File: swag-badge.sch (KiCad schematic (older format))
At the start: 7 parts

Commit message: Removed tinypico footprint :(
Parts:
- removed J?: Lolin32_Header_Left, symbol Connector_Generic:Conn_01x16
- removed J?: Lolin32_Header_Right, symbol Connector_Generic:Conn_01x20
- removed LEFT1, RIGHT1: TINYPICO_HEADER_10, Shield_Empty:1X10_NO_SILK, symbol swag-badge-rescue:TINYPICO_HEADER_10NO_SILK_PTH_FEMALE-Shield_Empty-eagle-import
- added J6: SAO_2, Pin_Headers:Pin_Header_Straight_2x03_Pitch2.54mm, symbol Connector_Generic:Conn_02x03_Counter_Clockwise
- added J?: Lolin32, symbol Connector_Generic:Conn_02x13_Counter_Clockwise
- added J?: SAO_3, Pin_Headers:Pin_Header_Straight_2x03_Pitch2.54mm, symbol Connector_Generic:Conn_02x03_Counter_Clockwise
- J1, J2: renamed from J?; footprint (none) -> Pin_Headers:Pin_Header_Straight_1x04_Pitch2.54mm
- J5: renamed from J?; footprint (none) -> Pin_Headers:Pin_Header_Straight_2x03_Pitch2.54mm
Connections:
- net labels added: EN, GPIO0, GPIO12, GPIO13, GPIO16, GPIO17, GPIO2, GPIO34, GPIO35, VN, VP
- net labels removed: +5V, 3.3V, GPIO21, RESET, USB, VBAT
- wire segments 44 -> 64
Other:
- moved on the sheet: J1, J2, J5

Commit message: Footprints associated
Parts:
- J1, J2: footprint Pin_Headers:Pin_Header_Straight_1x04_Pitch2.54mm -> SwagBadge:Display_Module_128X64_I2C_SSD1306
- J3: renamed from J?; footprint (none) -> SwagBadge:LOLIN32_Flipped_SmallCut
- J4: renamed from J?; footprint Pin_Headers:Pin_Header_Straight_2x03_Pitch2.54mm -> SwagBadge:SAO_Header_6-Pin
- J5, J6: footprint Pin_Headers:Pin_Header_Straight_2x03_Pitch2.54mm -> SwagBadge:SAO_Header_6-Pin
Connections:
- net +3V3: now also J3.14 (Pin_14); no longer J3.26 (Pin_26)
- net EN: now also J3.11 (Pin_11); no longer J3.3 (Pin_3)
- net GND: now also J3.1 (Pin_1); no longer J3.13 (Pin_13)
- net GPIO0: now also J3.23 (Pin_23); no longer J3.17 (Pin_17)
- net GPIO12: now also J3.2 (Pin_2); no longer J3.12 (Pin_12)
- net GPIO13: now also J3.26 (Pin_26); no longer J3.14 (Pin_14)
- net GPIO14: now also J3.3 (Pin_3); no longer J3.11 (Pin_11)
- net GPIO15: now also J3.25 (Pin_25); no longer J3.15 (Pin_15)
- net GPIO16: now also J3.21 (Pin_21); no longer J3.19 (Pin_19)
- net GPIO18: now also J3.18 (Pin_18); no longer J3.22 (Pin_22)
- net GPIO19: now also J3.16 (Pin_16); no longer J3.24 (Pin_24)
- net GPIO2: now also J3.24 (Pin_24); no longer J3.16 (Pin_16)
- net GPIO22: now also J3.15 (Pin_15); no longer J3.25 (Pin_25)
- net GPIO23: now also J3.17 (Pin_17); no longer J3.23 (Pin_23)
- net GPIO25: now also J3.6 (Pin_6); no longer J3.8 (Pin_8)
- net GPIO26: now also J3.5 (Pin_5); no longer J3.9 (Pin_9)
- net GPIO27: now also J3.4 (Pin_4); no longer J3.10 (Pin_10)
- net GPIO32: now also J3.8 (Pin_8); no longer J3.6 (Pin_6)
- net GPIO34: now also J3.10 (Pin_10); no longer J3.4 (Pin_4)
- net GPIO35: now also J3.9 (Pin_9); no longer J3.5 (Pin_5)
- net GPIO4: now also J3.22 (Pin_22); no longer J3.18 (Pin_18)
- net GPIO5: now also J3.19 (Pin_19); no longer J3.21 (Pin_21)
- net VN: now also J3.12 (Pin_12); no longer J3.2 (Pin_2)
- net VP: now also J3.13 (Pin_13); no longer J3.1 (Pin_1)
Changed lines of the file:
@@
 F 0 "J1" H 3268 4867 50  0000 C CNN
 F 1 "OLED_1" H 3268 4776 50  0000 C CNN
-F 2 "Pin_Headers:Pin_Header_Straight_1x04_Pitch2.54mm" H 3350 4550 50  0001 C CNN
+F 2 "SwagBadge:Display_Module_128X64_I2C_SSD1306" H 3350 4550 50  0001 C CNN
 F 3 "~" H 3350 4550 50  0001 C CNN
 	1    3350 4550
@@
 F 0 "J2" H 3268 5667 50  0000 C CNN
 F 1 "OLED_2" H 3268 5576 50  0000 C CNN
-F 2 "Pin_Headers:Pin_Header_Straight_1x04_Pitch2.54mm" H 3350 5350 50  0001 C CNN
+F 2 "SwagBadge:Display_Module_128X64_I2C_SSD1306" H 3350 5350 50  0001 C CNN
 F 3 "~" H 3350 5350 50  0001 C CNN
 	1    3350 5350
@@
 F 0 "J5" H 4050 1467 50  0000 C CNN
 F 1 "SAO_1" H 4050 1376 50  0000 C CNN
-F 2 "Pin_Headers:Pin_Header_Straight_2x03_Pitch2.54mm" H 4000 1150 50  0001 C CNN
+F 2 "SwagBadge:SAO_Header_6-Pin" H 4000 1150 50  0001 C CNN
 F 3 "~" H 4000 1150 50  0001 C CNN
 	1    4000 1150
@@
 F 0 "J6" H 4050 2417 50  0000 C CNN
 F 1 "SAO_2" H 4050 2326 50  0000 C CNN
-F 2 "Pin_Headers:Pin_Header_Straight_2x03_Pitch2.54mm" H 4000 2100 50  0001 C CNN
+F 2 "SwagBadge:SAO_Header_6-Pin" H 4000 2100 50  0001 C CNN
 F 3 "~" H 4000 2100 50  0001 C CNN
 	1    4000 2100
@@
 $EndComp
 $Comp
-L Connector_Generic:Conn_02x13_Counter_Clockwise J?
+L Connector_Generic:Conn_02x13_Counter_Clockwise J3
 U 1 1 5F73663E
 P 1800 2000
-F 0 "J?" H 1850 2817 50  0000 C CNN
+F 0 "J3" H 1850 2817 50  0000 C CNN
 F 1 "Lolin32" H 1850 2726 50  0000 C CNN
-F 2 "" H 1800 2000 50  0001 C CNN
+F 2 "SwagBadge:LOLIN32_Flipped_SmallCut" H 1800 2000 50  0001 C CNN
 F 3 "~" H 1800 2000 50  0001 C CNN
 	1    1800 2000
-	1    0    0    -1
+	1    0    0    1
 $EndComp
 Wire Wire Line
@@
 	2100 1500 2500 1500
 $Comp
-L Connector_Generic:Conn_02x03_Counter_Clockwise J?
+L Connector_Generic:Conn_02x03_Counter_Clockwise J4
 U 1 1 5F7685A3
 P 4000 3100
-F 0 "J?" H 4050 3417 50  0000 C CNN
+F 0 "J4" H 4050 3417 50  0000 C CNN
 F 1 "SAO_3" H 4050 3326 50  0000 C CNN
-F 2 "Pin_Headers:Pin_Header_Straight_2x03_Pitch2.54mm" H 4000 3100 50  0001 C CNN
+F 2 "SwagBadge:SAO_Header_6-Pin" H 4000 3100 50  0001 C CNN
 F 3 "~" H 4000 3100 50  0001 C CNN
 	1    4000 3100
@@
 $EndComp
 $Comp
-L power:GND #PWR?
+L power:GND #PWR0101
 U 1 1 5F7685AD
 P 4800 3350
-F 0 "#PWR?" H 4800 3100 50  0001 C CNN
+F 0 "#PWR0101" H 4800 3100 50  0001 C CNN
 F 1 "GND" H 4805 3177 50  0000 C CNN
 F 2 "" H 4800 3350 50  0001 C CNN
@@
 	4300 3200 4750 3200
 $Comp
-L power:+3V3 #PWR?
+L power:+3V3 #PWR0102
 U 1 1 5F7685C1
 P 3700 2900
-F 0 "#PWR?" H 3700 2750 50  0001 C CNN
+F 0 "#PWR0102" H 3700 2750 50  0001 C CNN
 F 1 "+3V3" H 3715 3073 50  0000 C CNN
 F 2 "" H 3700 2900 50  0001 C CNN

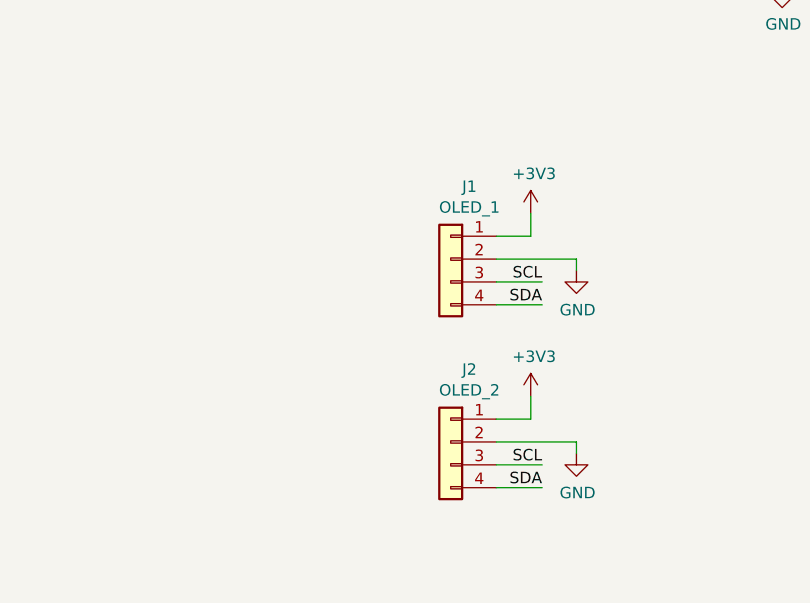
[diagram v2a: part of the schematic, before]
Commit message: Tactile buttons added
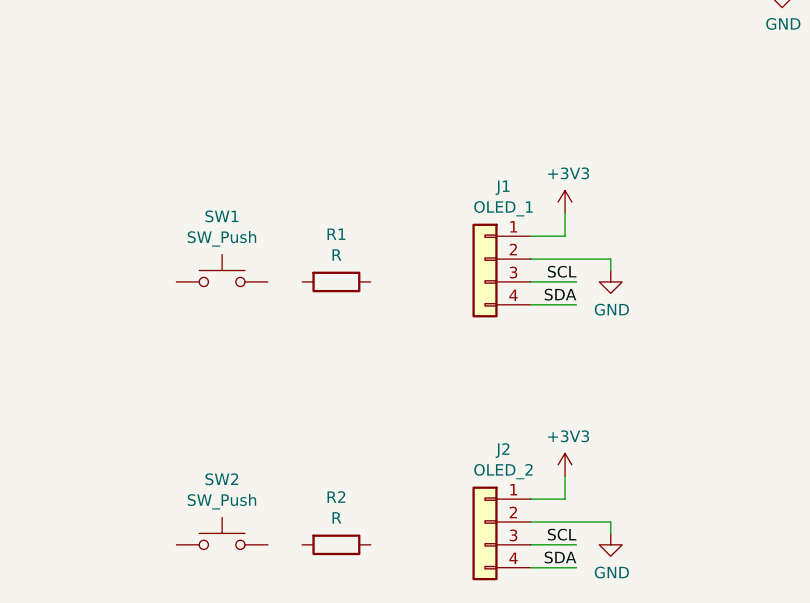
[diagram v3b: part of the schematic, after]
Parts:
- added R1, R2: R, Resistors_SMD:R_0805, symbol Device:R
- added SW1, SW2: SW_Push, SwagBadge:SW_SPST_6-3x3mm, symbol Switch:SW_Push
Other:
- moved on the sheet: J1, J2
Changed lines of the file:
@@
 L Connector_Generic:Conn_01x04 J1
 U 1 1 5F5375FF
-P 3350 4550
-F 0 "J1" H 3268 4867 50  0000 C CNN
-F 1 "OLED_1" H 3268 4776 50  0000 C CNN
-F 2 "SwagBadge:Display_Module_128X64_I2C_SSD1306" H 3350 4550 50  0001 C CNN
-F 3 "~" H 3350 4550 50  0001 C CNN
-	1    3350 4550
+P 3500 4550
+F 0 "J1" H 3418 4867 50  0000 C CNN
+F 1 "OLED_1" H 3418 4776 50  0000 C CNN
+F 2 "SwagBadge:Display_Module_128X64_I2C_SSD1306" H 3500 4550 50  0001 C CNN
+F 3 "~" H 3500 4550 50  0001 C CNN
+	1    3500 4550
 	-1   0    0    -1
 $EndComp
@@
 L Connector_Generic:Conn_01x04 J2
 U 1 1 5F53A38D
-P 3350 5350
-F 0 "J2" H 3268 5667 50  0000 C CNN
-F 1 "OLED_2" H 3268 5576 50  0000 C CNN
-F 2 "SwagBadge:Display_Module_128X64_I2C_SSD1306" H 3350 5350 50  0001 C CNN
-F 3 "~" H 3350 5350 50  0001 C CNN
-	1    3350 5350
+P 3500 5700
+F 0 "J2" H 3418 6017 50  0000 C CNN
+F 1 "OLED_2" H 3418 5926 50  0000 C CNN
+F 2 "SwagBadge:Display_Module_128X64_I2C_SSD1306" H 3500 5700 50  0001 C CNN
+F 3 "~" H 3500 5700 50  0001 C CNN
+	1    3500 5700
 	-1   0    0    -1
 $EndComp
@@
 L power:+3V3 #PWR0106
 U 1 1 5F53F1EB
-P 3700 4350
-F 0 "#PWR0106" H 3700 4200 50  0001 C CNN
-F 1 "+3V3" H 3715 4523 50  0000 C CNN
-F 2 "" H 3700 4350 50  0001 C CNN
-F 3 "" H 3700 4350 50  0001 C CNN
-	1    3700 4350
-	1    0    0    -1
-$EndComp
-Text Label 3750 4750 2    50   ~ 0
-SDA
-Text Label 3750 4650 2    50   ~ 0
-SCL
-Wire Wire Line
-	3550 4650 3750 4650
-Wire Wire Line
-	3550 4750 3750 4750
-Wire Wire Line
-	3550 4450 3700 4450
-Wire Wire Line
-	3700 4450 3700 4350
+P 3850 4350
+F 0 "#PWR0106" H 3850 4200 50  0001 C CNN
+F 1 "+3V3" H 3865 4523 50  0000 C CNN
+F 2 "" H 3850 4350 50  0001 C CNN
+F 3 "" H 3850 4350 50  0001 C CNN
+	1    3850 4350
+	1    0    0    -1
+$EndComp
+Text Label 3900 4750 2    50   ~ 0
+SDA
+Text Label 3900 4650 2    50   ~ 0
+SCL
+Wire Wire Line
+	3700 4650 3900 4650
+Wire Wire Line
+	3700 4750 3900 4750
+Wire Wire Line
+	3700 4450 3850 4450
+Wire Wire Line
+	3850 4450 3850 4350
 $Comp
 L power:GND #PWR0107
 U 1 1 5F5403D5
-P 3900 4600
-F 0 "#PWR0107" H 3900 4350 50  0001 C CNN
-F 1 "GND" H 3905 4427 50  0000 C CNN
-F 2 "" H 3900 4600 50  0001 C CNN
-F 3 "" H 3900 4600 50  0001 C CNN
-	1    3900 4600
-	1    0    0    -1
-$EndComp
-Wire Wire Line
-	3550 4550 3900 4550
-Wire Wire Line
-	3900 4550 3900 4600
+P 4050 4600
+F 0 "#PWR0107" H 4050 4350 50  0001 C CNN
+F 1 "GND" H 4055 4427 50  0000 C CNN
+F 2 "" H 4050 4600 50  0001 C CNN
+F 3 "" H 4050 4600 50  0001 C CNN
+	1    4050 4600
+	1    0    0    -1
+$EndComp
+Wire Wire Line
+	3700 4550 4050 4550
+Wire Wire Line
+	4050 4550 4050 4600
 $Comp
 L power:+3V3 #PWR0108
 U 1 1 5F540D5F
-P 3700 5150
-F 0 "#PWR0108" H 3700 5000 50  0001 C CNN
-F 1 "+3V3" H 3715 5323 50  0000 C CNN
-F 2 "" H 3700 5150 50  0001 C CNN
-F 3 "" H 3700 5150 50  0001 C CNN
-	1    3700 5150
-	1    0    0    -1
-$EndComp
-Text Label 3750 5550 2    50   ~ 0
-SDA
-Text Label 3750 5450 2    50   ~ 0
-SCL
-Wire Wire Line
-	3550 5450 3750 5450
-Wire Wire Line
-	3550 5550 3750 5550
-Wire Wire Line
-	3550 5250 3700 5250
-Wire Wire Line
-	3700 5250 3700 5150
+P 3850 5500
+F 0 "#PWR0108" H 3850 5350 50  0001 C CNN
+F 1 "+3V3" H 3865 5673 50  0000 C CNN
+F 2 "" H 3850 5500 50  0001 C CNN
+F 3 "" H 3850 5500 50  0001 C CNN
+	1    3850 5500
+	1    0    0    -1
+$EndComp
+Text Label 3900 5900 2    50   ~ 0
+SDA
+Text Label 3900 5800 2    50   ~ 0
+SCL
+Wire Wire Line
+	3700 5800 3900 5800
+Wire Wire Line
+	3700 5900 3900 5900
+Wire Wire Line
+	3700 5600 3850 5600
+Wire Wire Line
+	3850 5600 3850 5500
 $Comp
 L power:GND #PWR0109
 U 1 1 5F540D6F
-P 3900 5400
-F 0 "#PWR0109" H 3900 5150 50  0001 C CNN
-F 1 "GND" H 3905 5227 50  0000 C CNN
-F 2 "" H 3900 5400 50  0001 C CNN
-F 3 "" H 3900 5400 50  0001 C CNN
-	1    3900 5400
-	1    0    0    -1
-$EndComp
-Wire Wire Line
-	3550 5350 3900 5350
-Wire Wire Line
-	3900 5350 3900 5400
+P 4050 5750
+F 0 "#PWR0109" H 4050 5500 50  0001 C CNN
+F 1 "GND" H 4055 5577 50  0000 C CNN
+F 2 "" H 4050 5750 50  0001 C CNN
+F 3 "" H 4050 5750 50  0001 C CNN
+	1    4050 5750
+	1    0    0    -1
+$EndComp
+Wire Wire Line
+	3700 5700 4050 5700
+Wire Wire Line
+	4050 5700 4050 5750
 $Comp
 L power:+3V3 #PWR0110
@@
 Text Label 3450 3200 0    70   ~ 0
 GPIO18
+$Comp
+L Switch:SW_Push SW1
+U 1 1 5F7A9FE9
+P 2350 4650
+F 0 "SW1" H 2350 4935 50  0000 C CNN
+F 1 "SW_Push" H 2350 4844 50  0000 C CNN
+F 2 "SwagBadge:SW_SPST_6-3x3mm" H 2350 4850 50  0001 C CNN
+F 3 "~" H 2350 4850 50  0001 C CNN
+	1    2350 4650
+	1    0    0    -1
+$EndComp
+$Comp
+L Device:R R1
+U 1 1 5F7B662C
+P 2850 4650
+F 0 "R1" V 2643 4650 50  0000 C CNN
+F 1 "R" V 2734 4650 50  0000 C CNN
+F 2 "Resistors_SMD:R_0805" V 2780 4650 50  0001 C CNN
+F 3 "~" H 2850 4650 50  0001 C CNN
+	1    2850 4650
+	0    1    1    0
+$EndComp
+$Comp
+L Switch:SW_Push SW2
+U 1 1 5F7BF1A3
+P 2350 5800
+F 0 "SW2" H 2350 6085 50  0000 C CNN
+F 1 "SW_Push" H 2350 5994 50  0000 C CNN
+F 2 "SwagBadge:SW_SPST_6-3x3mm" H 2350 6000 50  0001 C CNN
+F 3 "~" H 2350 6000 50  0001 C CNN
+	1    2350 5800
+	1    0    0    -1
+$EndComp
+$Comp
+L Device:R R2
+U 1 1 5F7BF1A9
+P 2850 5800
+F 0 "R2" V 2643 5800 50  0000 C CNN
+F 1 "R" V 2734 5800 50  0000 C CNN
+F 2 "Resistors_SMD:R_0805" V 2780 5800 50  0001 C CNN
+F 3 "~" H 2850 5800 50  0001 C CNN
+	1    2850 5800
+	0    1    1    0
+$EndComp
 $EndSCHEMATC

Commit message: Footprint renamed and reassociated
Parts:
- SW1, SW2: footprint SwagBadge:SW_SPST_6-3x3mm -> SwagBadge:SW_SPST_6x3mm
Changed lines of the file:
@@
 F 0 "SW1" H 2350 4935 50  0000 C CNN
 F 1 "SW_Push" H 2350 4844 50  0000 C CNN
-F 2 "SwagBadge:SW_SPST_6-3x3mm" H 2350 4850 50  0001 C CNN
+F 2 "SwagBadge:SW_SPST_6x3mm" H 2350 4850 50  0001 C CNN
 F 3 "~" H 2350 4850 50  0001 C CNN
 	1    2350 4650
@@
 F 0 "SW2" H 2350 6085 50  0000 C CNN
 F 1 "SW_Push" H 2350 5994 50  0000 C CNN
-F 2 "SwagBadge:SW_SPST_6-3x3mm" H 2350 6000 50  0001 C CNN
+F 2 "SwagBadge:SW_SPST_6x3mm" H 2350 6000 50  0001 C CNN
 F 3 "~" H 2350 6000 50  0001 C CNN
 	1    2350 5800
